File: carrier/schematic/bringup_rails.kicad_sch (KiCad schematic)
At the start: 25 parts, among them SW4001 DSHP04TSGER, SW4002 DSHP08TSGER, SW4003 TS-1187A-B-A-B, SW4004 TS-1187A-B-A-B, SW4005 TS-1187A-B-A-B, SW4006 DSHP04TSGER, U4001 TCA9535PWR

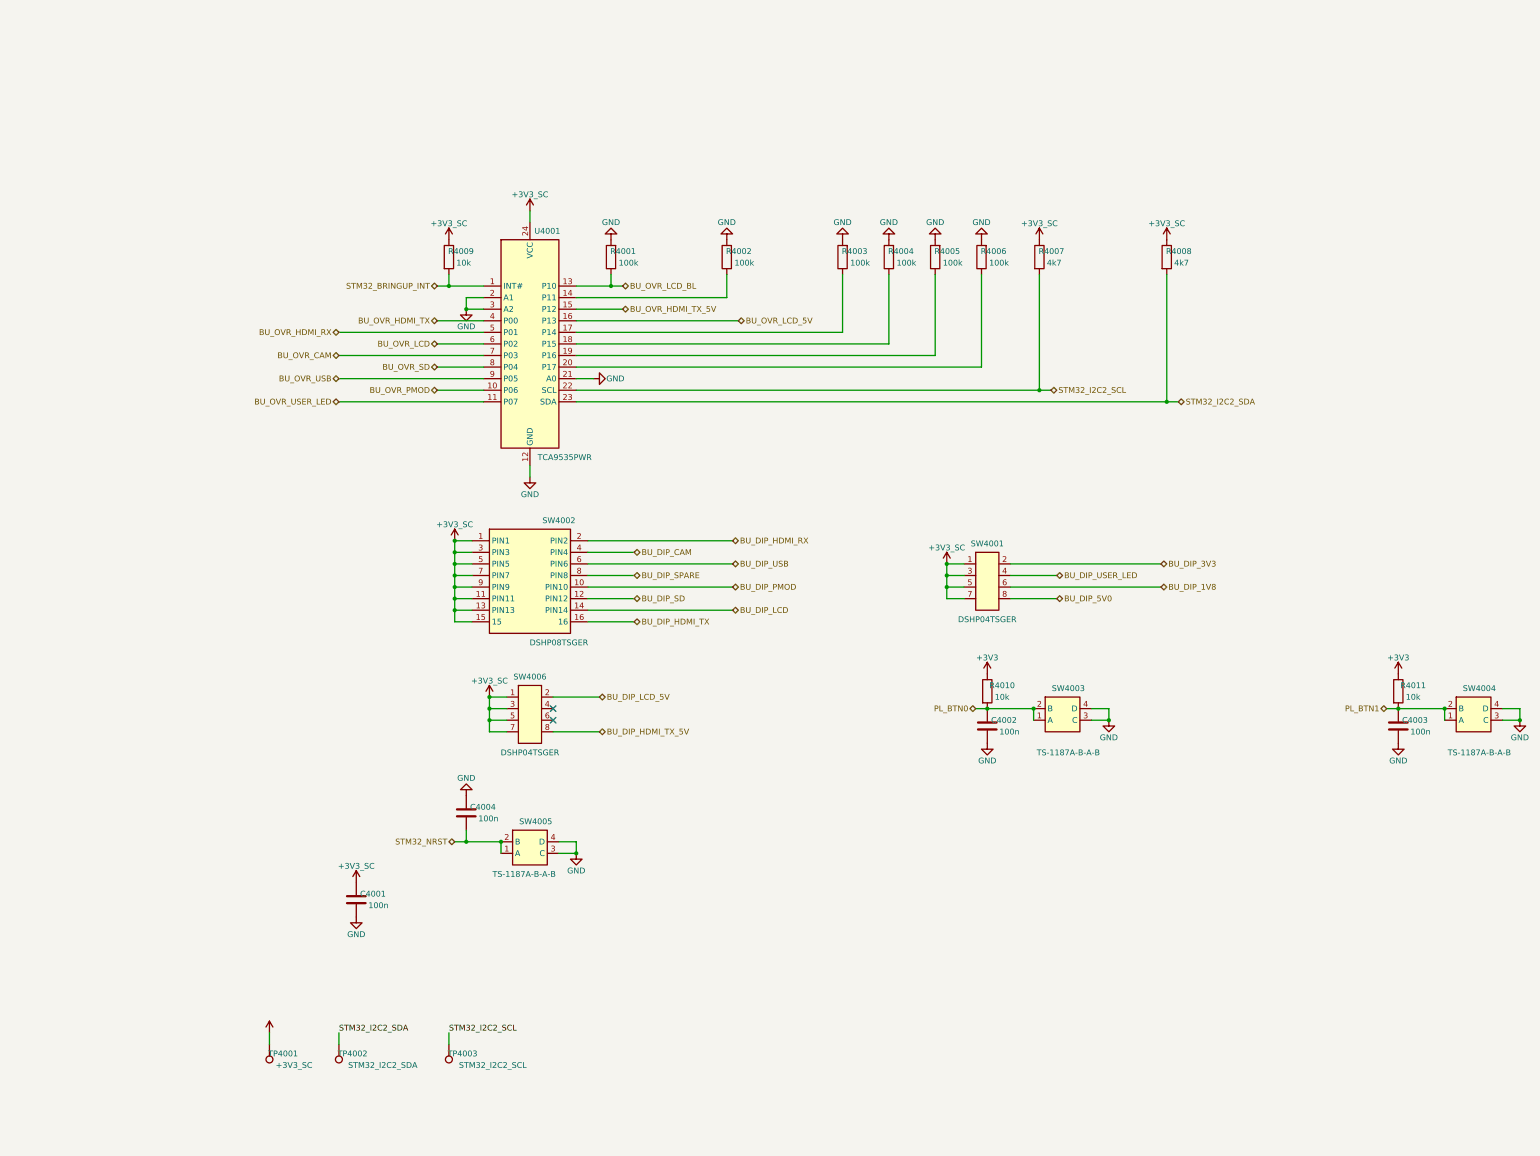
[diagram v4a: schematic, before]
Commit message: wave3(function-map): harvest — retire 109/121 cross-sheet deferrals
som_conn_gen FUNCTION_MAP emits carrier function names on J1/J2/J3 (RAIL_EN
GPIOs, SC_INT_N wire-OR [usb_pd R1 dropped, single +3V3_SC pull-up], bit-bang
I2C2 on DAC1/2, USBOTG_FLT_N->TCA9535 P14 with +3V3_SC re-rail abs-max fix,
PMON_ALERT->P11, SD_CD/LCD_CTP/HDMI/camera/FMC/PL_BTN binds, PUDC_34 strap,
VADJ 0.40->0.35A). xdc/firmware/link follow the same map. LINK 0 unbound,
12 intentionally-future deferrals (wave-2 RJ45/USB + EN_LCD_BL). Validated by
the HARDENED gates from the engine-fix harvest; goldens som_j2+bringup_rails
re-blessed after eyeball (clean); board byte-deterministic, selftest 44/44.

Co-Authored-By: Claude Fable 5 <noreply@anthropic.com>
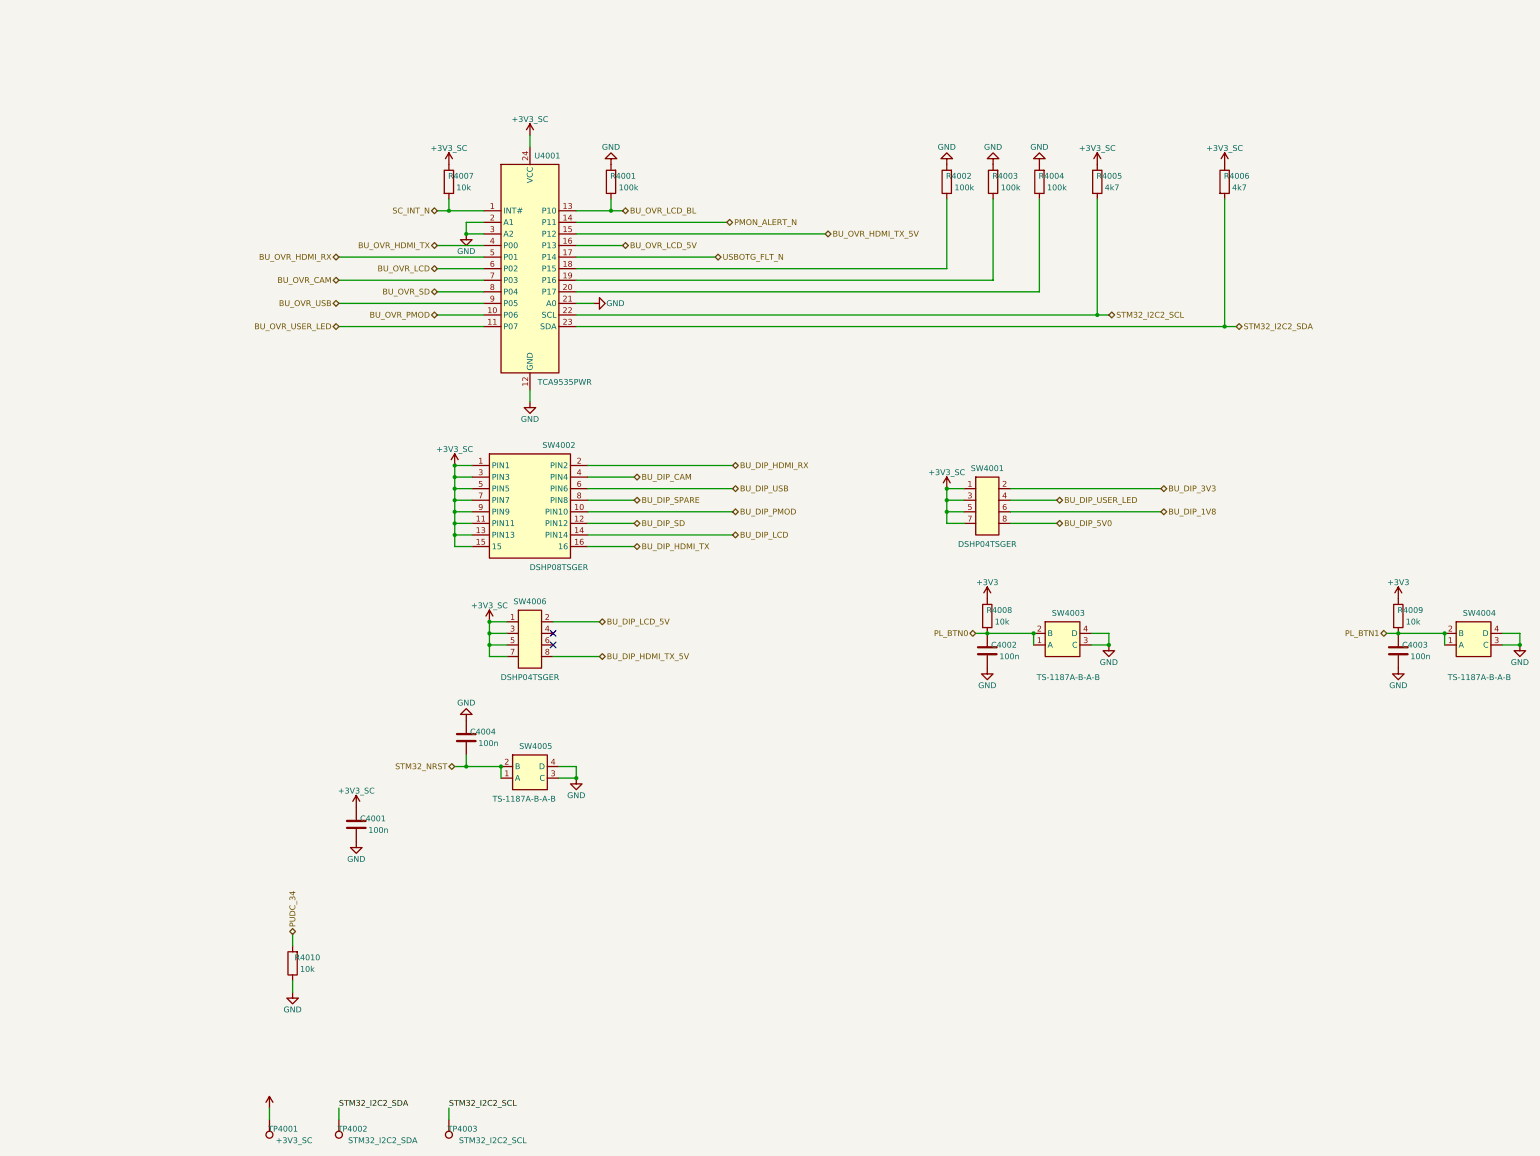
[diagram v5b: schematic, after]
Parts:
- removed TP4003: STM32_I2C2_SCL, TestPoint:TestPoint_Pad_D1.5mm, symbol Connector:TestPoint
- C4001: renamed from SW4005; value TS-1187A-B-A-B -> 100n; footprint TS-1187A-B-A-B:TS-1187A-B-A-B -> Capacitor_SMD:C_0603_1608Metric; symbol TS-1187A-B-A-B:TS-1187A-B-A-B -> Device:C; LCSC C318884 -> C1591
- C4002: renamed from SW4003; value TS-1187A-B-A-B -> 100n; footprint TS-1187A-B-A-B:TS-1187A-B-A-B -> Capacitor_SMD:C_0603_1608Metric; symbol TS-1187A-B-A-B:TS-1187A-B-A-B -> Device:C; LCSC C318884 -> C1591
- C4003: renamed from SW4004; value TS-1187A-B-A-B -> 100n; footprint TS-1187A-B-A-B:TS-1187A-B-A-B -> Capacitor_SMD:C_0603_1608Metric; symbol TS-1187A-B-A-B:TS-1187A-B-A-B -> Device:C; LCSC C318884 -> C1591
- R4005, R4006: value 100k -> 4k7; LCSC C25803 -> C23162
- R4008: renamed from SW4006; value DSHP04TSGER -> 10k; footprint DSHP04TSGER:DSHP04TSGER -> Resistor_SMD:R_0603_1608Metric; symbol DSHP04TSGER:DSHP04TSGER -> Device:R; LCSC C3293144 -> C25804
- R4009: renamed from C4002; value 100n -> 10k; footprint Capacitor_SMD:C_0603_1608Metric -> Resistor_SMD:R_0603_1608Metric; symbol Device:C -> Device:R; LCSC C1591 -> C25804
- R4010: renamed from C4004; value 100n -> 10k; footprint Capacitor_SMD:C_0603_1608Metric -> Resistor_SMD:R_0603_1608Metric; symbol Device:C -> Device:R; LCSC C1591 -> C25804
- SW4001: renamed from R4008; value 4k7 -> DSHP04TSGER; footprint Resistor_SMD:R_0603_1608Metric -> DSHP04TSGER:DSHP04TSGER; symbol Device:R -> DSHP04TSGER:DSHP04TSGER; LCSC C23162 -> C3293144
- SW4002: renamed from R4007; value 4k7 -> DSHP08TSGER; footprint Resistor_SMD:R_0603_1608Metric -> DSHP08TSGER:DSHP08TSGER; symbol Device:R -> DSHP08TSGER:DSHP08TSGER; LCSC C23162 -> C3293147
- SW4003: renamed from SW4001; value DSHP04TSGER -> TS-1187A-B-A-B; footprint DSHP04TSGER:DSHP04TSGER -> TS-1187A-B-A-B:TS-1187A-B-A-B; symbol DSHP04TSGER:DSHP04TSGER -> TS-1187A-B-A-B:TS-1187A-B-A-B; LCSC C3293144 -> C318884
- SW4004: renamed from R4010; value 10k -> TS-1187A-B-A-B; footprint Resistor_SMD:R_0603_1608Metric -> TS-1187A-B-A-B:TS-1187A-B-A-B; symbol Device:R -> TS-1187A-B-A-B:TS-1187A-B-A-B; LCSC C25804 -> C318884
- SW4005: renamed from R4011; value 10k -> TS-1187A-B-A-B; footprint Resistor_SMD:R_0603_1608Metric -> TS-1187A-B-A-B:TS-1187A-B-A-B; symbol Device:R -> TS-1187A-B-A-B:TS-1187A-B-A-B; LCSC C25804 -> C318884
- SW4006: renamed from SW4002; value DSHP08TSGER -> DSHP04TSGER; footprint DSHP08TSGER:DSHP08TSGER -> DSHP04TSGER:DSHP04TSGER; symbol DSHP08TSGER:DSHP08TSGER -> DSHP04TSGER:DSHP04TSGER; LCSC C3293147 -> C3293144
- TP4001: renamed from C4001; value 100n -> +3V3_SC; footprint Capacitor_SMD:C_0603_1608Metric -> TestPoint:TestPoint_Pad_D1.5mm; symbol Device:C -> Connector:TestPoint; BOM (none) -> exclude; LCSC C1591 -> (none)
- TP4002: renamed from TP4001; value +3V3_SC -> STM32_I2C2_SDA
- TP4003: renamed from TP4002; value STM32_I2C2_SDA -> STM32_I2C2_SCL
- renumbered C4003 to C4004, R4009 to R4007
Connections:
- net +3V3: now also R4008.1, R4009.1; no longer SW4004.1, SW4005.1
- net +3V3_SC: now also C4001.1, R4005.1, R4006.1, SW4001.3, SW4001.5, SW4001.7, SW4002.11 (PIN11), SW4002.13 (PIN13), SW4002.15, SW4002.3 (PIN3), SW4002.5 (PIN5), SW4002.7 (PIN7), SW4002.9 (PIN9); no longer R4008.1, R4008.3, R4008.5, R4008.7, SW4003.1, SW4003.3, SW4003.5, SW4003.7, SW4006.11 (PIN11), SW4006.13 (PIN13), SW4006.15, SW4006.9 (PIN9), TP4002.1
- net BU_DIP_1V8: now also SW4001.6; no longer SW4003.6
- net BU_DIP_3V3: now also SW4001.2; no longer SW4003.2
- net BU_DIP_5V0: now also SW4001.8; no longer SW4003.8
- net BU_DIP_CAM: now also SW4002.4 (PIN4); no longer SW4006.4 (PIN4)
- net BU_DIP_HDMI_RX: now also SW4002.2 (PIN2); no longer SW4006.2 (PIN2)
- net BU_DIP_HDMI_TX: now also SW4002.16; no longer SW4006.16
- net BU_DIP_HDMI_TX_5V: now also SW4006.8; no longer R4008.8
- net BU_DIP_LCD: now also SW4002.14 (PIN14); no longer SW4006.14 (PIN14)
- net BU_DIP_LCD_5V: now also SW4006.2; no longer R4008.2
- net BU_DIP_PMOD: now also SW4002.10 (PIN10); no longer SW4006.10 (PIN10)
- net BU_DIP_SD: now also SW4002.12 (PIN12); no longer SW4006.12 (PIN12)
- net BU_DIP_SPARE: now also SW4002.8 (PIN8); no longer SW4006.8 (PIN8)
- net BU_DIP_USB: now also SW4002.6 (PIN6); no longer SW4006.6 (PIN6)
- net BU_DIP_USER_LED: now also SW4001.4; no longer SW4003.4
- net GND: now also C4001.2, C4002.2, C4003.2, R4010.1, SW4003.3 (C), SW4003.4 (D), SW4004.3 (C), SW4004.4 (D), SW4005.3 (C), SW4005.4 (D); no longer C4001.3 (C), C4001.4 (D), C4002.3 (C), C4002.4 (D), C4003.3 (C), C4003.4 (D), R4005.2, R4006.2, R4009.2, R4010.2, TP4001.2
- net PL_BTN0: now also R4008.2, SW4003.1 (A), SW4003.2 (B); no longer C4002.2 (B), R4009.1, SW4004.2
- net PL_BTN1: now also R4009.2, SW4004.1 (A), SW4004.2 (B); no longer C4003.2 (B), C4004.1, SW4005.2
- net STM32_I2C2_SCL: now also R4005.2, TP4003.1; no longer SW4002.2
- net STM32_I2C2_SDA: now also R4006.2, TP4002.1; no longer SW4001.2, TP4003.1
- net STM32_NRST: now also C4004.1, SW4005.1 (A), SW4005.2 (B); no longer C4001.1 (A), C4001.2 (B), R4010.1
- net at R4004.1: now also U4001.20 (P17); no longer U4001.18 (P15)
- net at R4003.1: now also U4001.19 (P16); no longer U4001.17 (P14)
- net at R4002.1: now also U4001.18 (P15); no longer U4001.14 (P11)
- net STM32_BRINGUP_INT renamed SC_INT_N
- new net PMON_ALERT_N: U4001.14 (P11)
- new net PUDC_34: R4010.2
- new net USBOTG_FLT_N: U4001.17 (P14)
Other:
- moved on the sheet: C4004, R4001, R4002, R4003, R4004, R4005, R4006, R4007, TP4002, TP4003, U4001

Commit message: genpolish: TITLE-1 — populate the schematic title block on every sheet
Every sheet rendered a blank Title/Rev/Date — the clearest 'not a real
schematic' tell. emit() now writes a (title_block ...) after the paper node:
title = the sheet circuit's title, company "Zynq SoM Carrier", and a
"<sheet> — generated by schgen (do not hand-edit)" comment. NO date node — a
wall-clock date would break byte-determinism; the content-derived fields keep
every rebuild identical. Verified on A4 (usb_pd) and the dense A3 (power): the
block fills the standard reserved corner with zero drawing overlap. All 26
sheets, goldens re-blessed, board PASS + deterministic, selftest 53/53, m1,
pytest 147.

Co-Authored-By: Claude Opus 4.8 <noreply@anthropic.com>
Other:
- company: (none) -> Zynq SoM Carrier
- title: (none) -> Bring-up controls: rail/module DIPs + TCA9535 + buttons
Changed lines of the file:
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@@
 	(generator_version "1.0")
 	(paper "A3")
+	(title_block
+		(title "Bring-up controls: rail/module DIPs + TCA9535 + buttons")
+		(company "Zynq SoM Carrier")
+		(comment 1 "bringup_rails — generated by schgen (do not hand-edit)")
+	)
 	(wire
 		(pts

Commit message: board: four board-management HW blocks on a manually-gated +3V3_AUX (BOARDHW)
The four services the carrier was missing — all behind ONE manual power enable
(C1) on two new sheets split so neither defeats the placer's rail-stub router:

  board_aux       — the gate + I2C isolator (infrastructure)
  board_services  — ID-EEPROM + RTC + watchdog + QWIIC (the peripherals)

WHAT LANDED
  * 24AA025E48 (C129895)  ID-EEPROM with a factory EUI-48 **MAC** for the
      LAN8720/RJ45 — strapped 0x51 (0x50 is the FMC EEPROM).
  * RV-3028-C7 (C3019759) I2C RTC, integrated DTCXO (no crystal), CR1220 coin
      cell (KH-CR1220-2) with auto-switchover, 0x52.
  * TPS3823-33 (C7719)    supervisor + windowed watchdog.
  * ZX-SH1.0-4PWT (C7430446)  QWIIC / STEMMA-QT expansion (gated 3V3 + the
      isolated AUX I2C).
  * SY6280 gate + DSHP04 DIP + PCA9306 isolator complete the infrastructure.

CONSTRAINTS (the user's three standing requirements)
  C1 manual enable "like the previous": +3V3_AUX is a SY6280 load switch whose
     EN is a default-OFF DSHP04 DIP (100k pulldown) — the same gated-module
     idiom, self-contained so it touches none of the dense rail/EN sheets.
  C2 "no watchdog reset during power-up": THREE independent guards — (1) the
     supervisor's VDD is the default-OFF +3V3_AUX, so it is UNPOWERED through
     power-up; (2) the TPS3823 disables its watchdog while WDI floats, and WDI
     is driven only by the PL (WATCHDOG_KICK, Hi-Z until the fabric is up); (3)
     RESET# is a firmware-mediated PL EVENT (J3.31), never a rail/POR line.
  C3 Zynq-agnostic: the only SoM-side signals (the 2 watchdog lines) ride PL
     bank-35 IO by their contract net names (IO_L16_N/P_35 -> J3.29/31); xdc.py
     emits the constraints live — nothing hard-codes the Zynq part.

LAW 0 (electrical integrity): the peripherals sit on the GATED rail but their
bus is the always-on STM32_I2C2 management bus. A PCA9306 bridges them with EN
tied to +3V3_AUX, so the switch OPENS whenever the rail is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
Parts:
- renumbered C4001 to C6001, C4002 to C6002, C4003 to C6003, C4004 to C6004, R4001 to R6001, R4002 to R6002, R4003 to R6003, R4004 to R6004, R4005 to R6005, R4006 to R6006, R4007 to R6007, R4008 to R6008, R4009 to R6009, R4010 to R6010, SW4001 to SW6001, SW4002 to SW6002, SW4003 to SW6003, SW4004 to SW6004, SW4005 to SW6005, SW4006 to SW6006, TP4001 to TP6001, TP4002 to TP6002, TP4003 to TP6003, U4001 to U6001

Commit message: audit fixes: QWIIC ESD on its own sheet + firmware I2C-map completeness
Acting on a multi-agent adversarial re-audit of the 28-sheet board. Each
finding was independently re-verified before action — two confident "HIGH"
findings were FALSE POSITIVES whose proposed fixes would have INTRODUCED bugs,
and are documented-rejected, not applied:

  * "DSHP04 switches in parallel" — wrong. The footprint pads prove the pairing
    by physical opposition (switch n = pads n & 9-n): switch 1 = pads 1&8 is the
    only one on EN_AUX; the other even pins (2/4/6) are NC, identical to the
    proven bringup_rails SW6 idiom. The proposed "fix" (pins 1+2) wires two
    DIFFERENT switches and would leave EN_AUX permanently pulled down — the rail
    could never enable.
  * "PCA9306 EN floats when AUX is off" — wrong. A 100k to a 0 V rail pulls EN
    to 0 V (disabled), which is exactly TI's recommended "isolate when the gated
    side is unpowered" connection. No float.

REAL findings actioned:

1. QWIIC connector lacked ESD (every other external connector has it). Moved the
   QWIIC out of board_services onto its own sheet board_qwiic (the carrier's
   connectors-get-their-own-sheet idiom — rj45_connector, usb_uart_connector)
   and added a USBLC6-2SC6 low-cap ESD array at the connector (1<->6 / 3<->4
   passthrough, clamp ref +3V3_AUX). The dedicated sheet also keeps both sheets
   sparse enough for the rail-stub router. board_services drops to 9 parts.

2. schgen/firmware.py loaded only 7 sheets, so the SC-firmware contract + its
   I2C address-collision check were BLIND to the new devices. Added board_aux/
   board_services to SOURCES and three address rows: FMC-EEPROM 0x50, ID-EEPROM
   0x51 (DERIVED from the 24AA025E48 A1/A0 straps, so a mis-strap to 0x50 now
   trips the collision check against the FMC EEPROM), RTC 0x52. The firmware can
   now address the EUI-48 MAC EEPROM and the RTC. 114 -> 117 #defines.

3. board_services docstring clarified (EEPROM/RTC are on the PCA9306-i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
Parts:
- renumbered C6001 to C7001, C6002 to C7002, C6003 to C7003, C6004 to C7004, R6001 to R7001, R6002 to R7002, R6003 to R7003, R6004 to R7004, R6005 to R7005, R6006 to R7006, R6007 to R7007, R6008 to R7008, R6009 to R7009, R6010 to R7010, SW6001 to SW7001, SW6002 to SW7002, SW6003 to SW7003, SW6004 to SW7004, SW6005 to SW7005, SW6006 to SW7006, TP6001 to TP7001, TP6002 to TP7002, TP6003 to TP7003, U6001 to U7001
